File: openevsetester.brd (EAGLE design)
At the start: 100 x 100 mm, 149 parts, among them IC1 LM321MF, Q10 BSS138, Q7 XTAL_CFPX-217

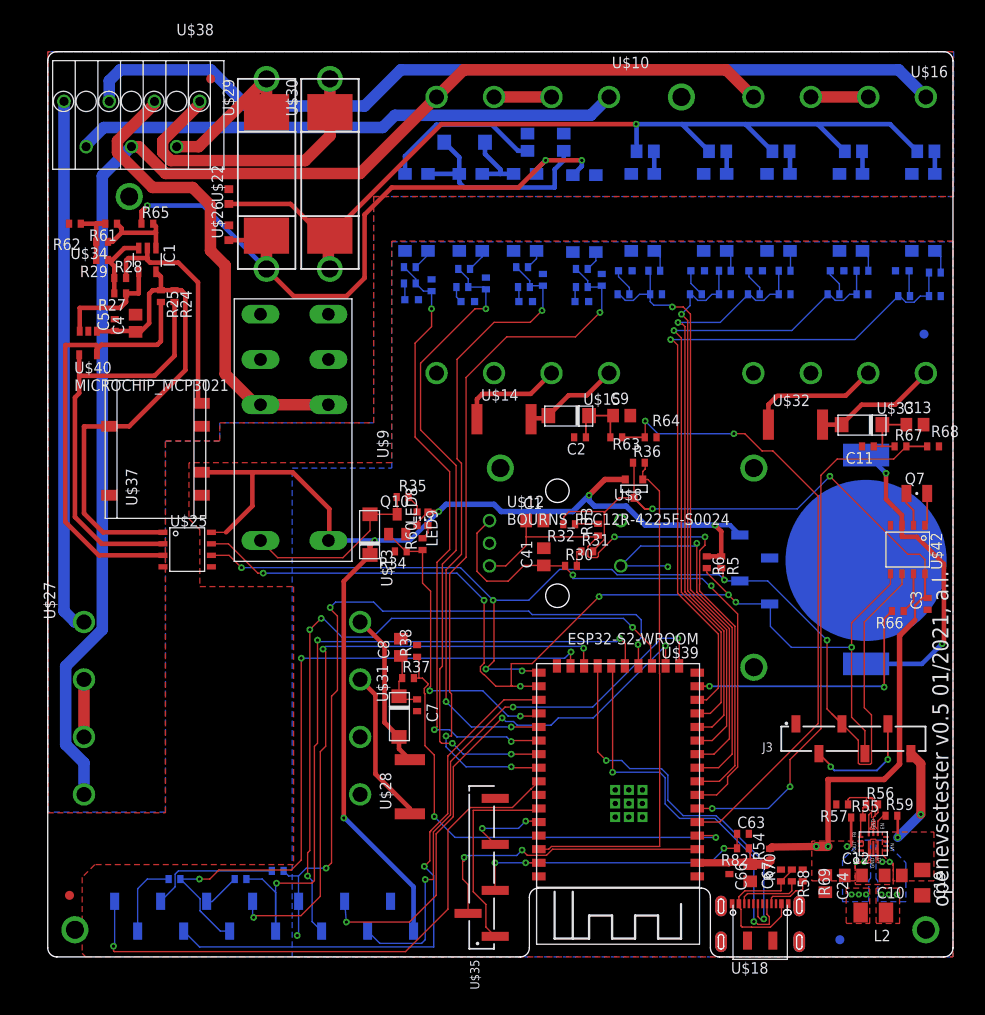
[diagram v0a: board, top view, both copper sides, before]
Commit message: isolated adc instead of dc/dc, op-amp and i2c isolator
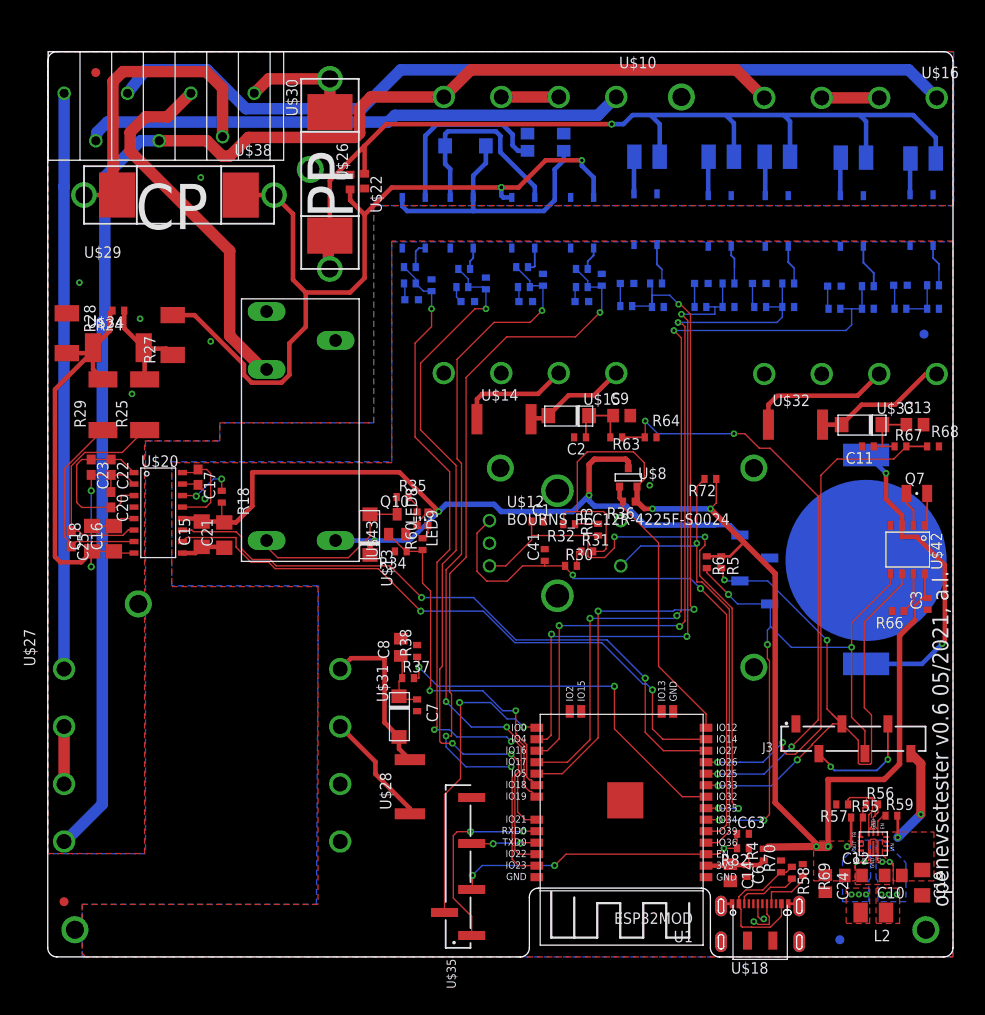
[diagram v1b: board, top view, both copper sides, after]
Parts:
- removed C4: 10u, resistor:C0805
- removed C5: 100n, resistor:C0402
- removed C66: 100n, rcl:C0402
- removed C67: 10u, rcl:C0805
- removed IC1: LM321MF, linear:SOT23-5
- removed J4: (no value), Wurth_Connectors_WR-PHD:61001413321
- removed R52, R53: 0R, resistor:R0402
- removed R54: 0k, resistor:R0402
- removed R61: 500k, resistor:R0402
- removed R62, R65: 1M 1% 0805 230v-safe, resistor:R0402
- removed U$25: ISO154X, mylib:SOIC-8
- removed U$37: RECOM_R0.25D-3.312, mylib:RECOM_RXS-RXD_6PIN
- removed U$39: ESP32-S2-WROOM, mylib:ESP32-S2-WROOM
- removed U$40: MICROCHIP_MCP3021, mylib:SOT23-5
- added C14: 10u, rcl:C0805
- added C15, C16: 1n, resistor:C1206
- added C17, C20: 100n, resistor:C0603
- added C18: 100n, resistor:C1206
- added C21: 1uF, resistor:C1206
- added C22: 1uF, resistor:C0603
- added C23: 1n, resistor:C0603
- added C25: 10n, resistor:C0603
- added C6: 100n, rcl:C0402
- added R72: 4k7, resistor:R0402
- added R73: 680R, resistor:R1210
- added U$43: OMRON_G6RL-14-ASI, mylib:OMRON_G6RL-14-ASI
- added U1: ESP32MOD, mylib:ESP32MOD
- C1, C41: device rcl:C0805 -> rcl:C0402
- R18: value 0R -> 47k
- R2: value 1k5 0,5W -> 1k5; device resistor:R0805 -> resistor:R1210
- R24: value 4k7 -> 10R 1% 400V; device resistor:R0402 -> resistor:R2512
- R25: value 4k7 -> 10R; device resistor:R0402 -> resistor:R2512
- R27: value 3k3 -> 237R 1% 400V; device resistor:R0402 -> resistor:R2010
- R28: value 10k -> 237R 1% 400V; device resistor:R0402 -> resistor:R2010
- R29: value 47k -> 10R; device resistor:R0402 -> resistor:R2512
- R3: value 220R 0,5W -> 220R; device resistor:R0805 -> resistor:R1210
- R4: value 680R 0,5W -> 0k; device resistor:R0805 -> resistor:R0402
- R7: value 4k7 0,5W -> 4k7; device resistor:R0805 -> resistor:R1210
- R8: value 100R 0,5W -> 100R; device resistor:R0805 -> resistor:R1210
- U$1, U$17, U$2, U$3, U$4, U$5, U$6, U$7: value RELAIS_MOSFET_OMRON_G3VM-351 -> IXYS_CPC1014N; device mylib:RELAIS_MOSFET_OMRON_G3VM-351 -> mylib:SOIC-4
- U$20: value RELAIS_MOSFET_OMRON_G3VM-351 -> AMC3306M25; device mylib:RELAIS_MOSFET_OMRON_G3VM-351 -> mylib:SOIC-16
- U$9: value OMRON_G5RL-U1-E-DC3 -> IXYS_CPC1014N; device mylib:OMRON_G5RL-U1-E -> mylib:SOIC-4
- moved R4 77.7 mm to (79.1, 11.3), flipped to the top, turned to 90 degrees
- moved U$9 48.9 mm to (67.3, 78.7), flipped to the bottom, turned to 0 degrees
- moved U$20 44.5 mm to (12.2, 51.6), flipped to the top, turned to 270 degrees
- moved R18 41.8 mm to (19.2, 50.8), flipped to the top, turned to 270 degrees
- moved U$29 23.3 mm to (4.00, 81.0), turned to 0 degrees
- moved R29 16.0 mm to (6.10, 61.0), turned to 90 degrees
- moved U$22 15.1 mm to (35.0, 85.7), turned to 270 degrees
- moved U$26 14.5 mm to (33.4, 85.6)
- moved U$19 12.7 mm to (5.30, 97.7)
- moved R25 12.1 mm to (10.7, 61.0), turned to 90 degrees
- moved R28 8.49 mm to (2.10, 68.9), turned to 270 degrees
- moved R24 8.42 mm to (7.80, 67.3), turned to 0 degrees
- moved U$34 7.81 mm to (7.80, 71.4)
- moved R27 7.40 mm to (13.8, 68.7), turned to 90 degrees
- moved U$6 7.01 mm to (47.0, 78.3)
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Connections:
- removed net +5V_ISOLATED: C4.1, C5.1, IC1.5, R24.1, R25.1, U$25.1, U$37.7, U$40.1
- removed net -5V_ISOLATED: IC1.2, R28.2, U$37.5
- removed net DISPLAY1: U$39.IO45
- removed net DISPLAY3: U$39.IO42
- removed net GND: C1.2, C10.2, C11.2, C12.2, C13.2, C19.2, C2.2, C24.2, C3.1, C41.2, C63.2, C66.2, C67.2, C7.2, C8.2, C9.2, J1.2, J3.1, J4.2, LED1.C, LED13.C, LED15.C, LED16.C, LED2.C, LED3.C, LED4.C, LED5.C, LED6.C, Q10.2, R10.1, R13.1, R16.1, R20.1, R22.1, R34.2, R38.2, R40.1, R43.1, R46.1, R50.1, R56.2, R57.2, R64.2, R68.2, R69.1, R70.2, U$1.2, U$12.2, U$12.C, U$17.2, U$18.A1/B12, U$18.A12/B1, U$18.G1, U$18.G2, U$18.G3, U$18.G4, U$18.G5, U$18.G6, U$18.G7, U$18.G8, U$18.P1, U$18.P2, U$2.2, U$20.2, U$25.5, U$3.2, U$35.7, U$36.GND, U$36.PGND, U$37.1, U$39.GND, U$39.GND1, U$39.GND2, U$39.PAD0, U$39.PAD1, U$39.PAD2, U$39.PAD3, U$39.PAD4, U$39.PAD5, U$39.PAD6, U$39.PAD7, U$39.PAD8, U$4.2, U$41.P$3, U$42.4, U$5.2, U$6.2, U$7.2
- removed net LCD_CS: J4.3, U$39.IO14
- removed net LCD_DC: J4.5, U$39.IO16
- removed net LCD_LED: J4.8, U$39.IO21
- removed net LCD_MISO: J4.9, R53.2, U$39.IO26
- removed net LCD_MOSI: J4.6, R18.1, U$39.IO17
- removed net LCD_RESET: J4.4, U$39.IO15
- removed net LCD_SCK: J4.7, R52.1, U$39.IO18
- removed net N$24: IC1.3, R27.2, R28.1, R29.1
- removed net N$27: IC1.4, R27.1, U$40.3
- removed net N$28: R24.2, U$25.2, U$40.4
- removed net N$29: R25.2, U$25.3, U$40.5
- removed net N$45: R29.2, R61.2, R62.1, U$34.2
- removed net TOUCH_CLK: J4.10, R52.2
- removed net TOUCH_CS: J4.11, U$39.IO35
- removed net TOUCH_D0: J4.13, R53.1
- removed net TOUCH_DIN: J4.12, R18.2
- removed net TOUCH_IRQ: J4.14, U$39.IO41
- new net AAA: C1.2, C10.2, C11.2, C12.2, C13.2, C14.2, C15.1, C17.2, C19.2, C2.2, C21.1, C24.2, C3.1, C41.2, C6.2, C63.2, C7.2, C8.2, C9.2, J1.2, J3.1, LED1.C, LED13.C, LED15.C, LED16.C, LED2.C, LED3.C, LED4.C, LED5.C, LED6.C, Q10.2, R10.1, R13.1, R16.1, R20.1, R22.1, R34.2, R38.2, R40.1, R43.1, R46.1, R50.1, R56.2, R57.2, R64.2, R68.2, R69.1, R70.2, U$1.2, U$12.2, U$12.C, U$12.GND1, U$12.GND2, U$17.2, U$18.A1/B12, U$18.A12/B1, U$18.G1, U$18.G2, U$18.G3, U$18.G4, U$18.G5, U$18.G6, U$18.G7, U$18.G8, U$18.P1, U$18.P2, U$2.2, U$20.15, U$20.9, U$3.2, U$35.7, U$36.GND, U$36.PGND, U$4.2, U$41.P$3, U$42.4, U$5.2, U$6.2, U$7.2, U$9.2, U1.0, U1.1, U1.15, U1.38
- new net ADC_CLKIN: U$20.11, U1.12
- new net ADC_DIAG: R18.1, U$20.14
- new net ADC_DOUT: U$20.10, U1.13
- new net N$37: C17.1, U$20.13, U$20.16
- new net N$42: C25.1, R25.1, U$20.6
- new net N$49: C25.2, R29.1, U$20.7
- new net N$50: C16.1, C18.1, C20.1, C22.2, C23.2, R24.1, R28.2, R29.2, U$20.2, U$20.8, U$34.2
- new net N$52: C16.2, C18.2, U$20.5
- new net N$54: C20.2, C22.1, C23.1, U$20.1, U$20.3
- net +3V3: now also C15.2, C21.2, R18.2, U$20.12, U$43.1, U$8.3; no longer J4.1, R5.1, R6.1, U$25.8, U$37.2, U$8.2, U$9.1
- net +3V3_PERMANENT: now also R4.2, R5.1, R6.1, R72.1, U$8.2; no longer R54.2, U$8.3
- net CP: now also R27.2, U$17.4; no longer R65.1, U$6.4
- net EN: now also U1.3; no longer U$39.EN
- net ESP32_VCC: now also C14.1, C6.1, R4.1, U1.2; no longer C66.1, C67.1, R54.1, U$39.3V3
- net GPIO0: now also U1.25; no longer U$39.IO0
- net GPIO_3V3_SWITCH: now also U1.14; no longer U$39.IO46
- net GPIO_L1: now also U1.8; no longer U$39.IO1
- net GPIO_L2: now also U1.10; no longer U$39.IO2
- net GPIO_L3: now also U1.11; no longer U$39.IO3
- net GPIO_PE_BREAKER: now also U1.30; no longer U$39.IO36
- net GPIO_PP1: now also U1.29; no longer U$39.IO7
- net GPIO_PP2: now also U1.26; no longer U$39.IO8
- net GPIO_PP3: now also U1.27; no longer U$39.IO9
- net GPIO_PP4: now also U1.28; no longer U$39.IO10
- net GPIO_PP5: no longer U$39.IO11
- net GPIO_ROTARY_A: now also U1.5; no longer U$39.IO4
- net GPIO_ROTARY_B: now also U1.7; no longer U$39.IO5
- net GPIO_ROTARY_BUTTON: now also R72.2, U1.4; no longer U$39.IO6
- net GPIO_RTC: no longer U$39.IO12
- net GPIO_STATE_AB: now also U1.31; no longer U$39.IO37
- net GPIO_STATE_C: now also U1.33; no longer U$39.IO38
- net GPIO_STATE_D_FAULT: now also U1.36; no longer U$39.IO39
- net GPIO_STATE_E: now also U1.37; no longer U$39.IO40
- net N$14: now also U$43.5; no longer U$9.8
- net N$16: now also U$9.1; no longer U$17.1
- net N$19: now also U$17.1; no longer U$5.1
- net N$20: now also U$5.1; no longer U$6.1
- net N$26: now also U$5.4; no longer U$20.4
- net N$31: now also U$6.1; no longer U$20.1
- net N$48: now also R24.2, R25.2, R27.1; no longer IC1.1, R61.1, R65.2
- net PE: now also R28.1, U$1.4, U$2.4, U$3.4, U$4.4, U$43.2, U$9.4; no longer C4.2, C5.2, R62.2, U$1.3, U$2.3, U$25.4, U$3.3, U$37.4, U$4.3, U$40.2, U$5.4, U$9.3, U$9.6
- net PE_IN: now also U$43.4; no longer U$9.2, U$9.7
- net PP: now also R73.2; no longer R4.2
- net PP1: now also U$9.3; no longer U$17.4
- net PP2: now also U$1.3; no longer U$1.4
- net PP3: now also R73.1, U$2.3; no longer R4.1, U$2.4
- net PP4: now also U$3.3; no longer U$3.4
- net PP5: now also U$4.3; no longer U$4.4
- net PP6: now also U$7.4; no longer U$7.3
- net PP7: now also U$6.4, U$7.3; no longer U$20.3, U$7.4
- net RXD: now also U1.34; no longer U$39.TXD0
- net SCL: now also U1.9; no longer U$25.6, U$39.IO33
- net SDA: now also U1.6; no longer U$25.7, U$39.IO34
- net TXD: now also U1.35; no longer U$39.RXD0
- net USB_D+: no longer U$39.IO20
- net USB_D-: no longer U$39.IO19
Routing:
- net LCD_MOSI: track 82.3 -> 0.00 mm, vias 4 -> 0
- net LCD_SCK: track 81.4 -> 0.00 mm, vias 3 -> 0
- net LCD_DC: track 77.5 -> 0.00 mm, vias 4 -> 0
- net LCD_MISO: track 76.8 -> 0.00 mm, vias 3 -> 0
- net GPIO_PP5: track 77.6 -> 4.90 mm, vias 1 -> 0
- net ADC_CLKIN: track 0.00 -> 72.2 mm, vias 0 -> 2
- net ADC_DOUT: track 0.00 -> 70.4 mm, vias 0 -> 2
- net LCD_LED: track 68.8 -> 0.00 mm, vias 3 -> 0
- net TOUCH_IRQ: track 65.5 -> 0.00 mm, vias 1 -> 0
- net N$50: track 0.00 -> 65.0 mm, vias 0 -> 2
- net TOUCH_CS: track 63.6 -> 0.00 mm, vias 1 -> 0
- net LCD_CS: track 62.3 -> 0.00 mm, vias 3 -> 0
- net LCD_RESET: track 60.3 -> 0.00 mm, vias 3 -> 0
- net +5V_ISOLATED: track 57.5 -> 0.00 mm
- net SCL: track 129.8 -> 73.0 mm, vias 6 -> 4
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- added copper zone on layer 1, net AAA
- added copper zone on layer 16, net AAA
- removed copper zone on layer 1, net GND
- removed copper zone on layer 16, net GND
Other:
- board text added: "CP"
- board text added: "PP"
- board text added: "openevsetester v0.6 05/2021, a.l."
- board text removed: "openevsetester v0.5 01/2021, a.l."
